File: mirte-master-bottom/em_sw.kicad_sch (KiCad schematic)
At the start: 13 parts, among them Q4 S8050 J3Y_C42441446, Q5 SiA483DJ, U11 DB125-2.54-2P-GN, U9 BZT52C18_C2932747

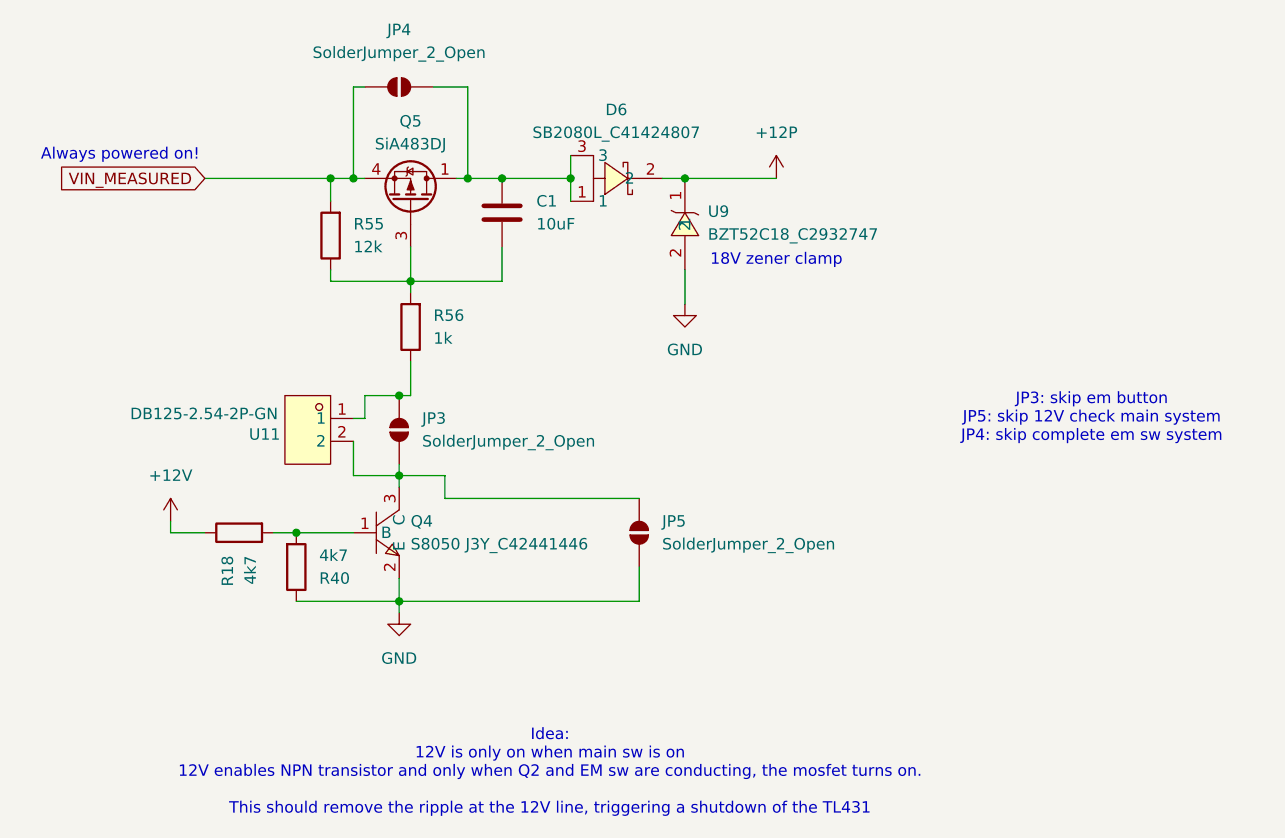
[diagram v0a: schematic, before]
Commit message: MM: ERC&DRC fixes + change hbridge cap
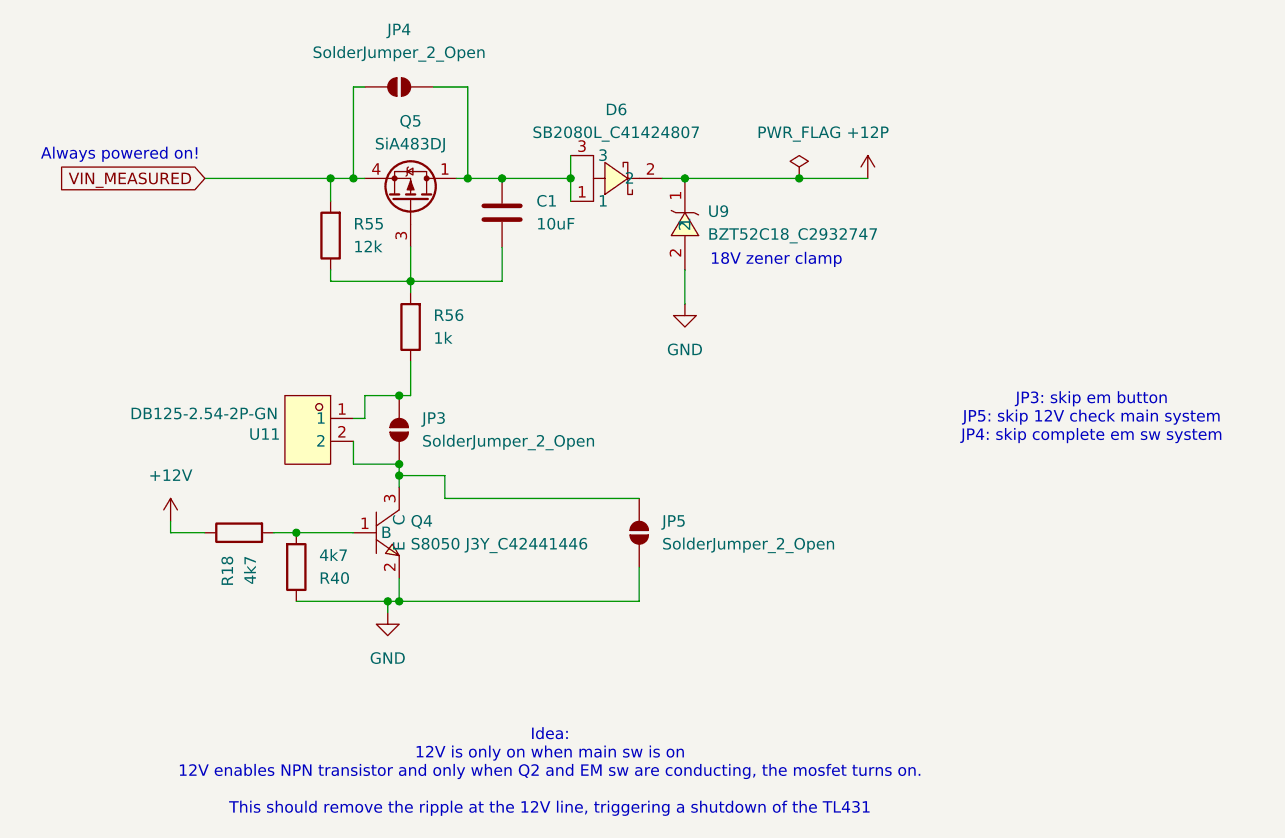
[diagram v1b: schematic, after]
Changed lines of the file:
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@@
+	)
+	(junction
+		(at 182.88 137.16)
+		(diameter 0)
+		(color 0 0 0 0)
 	)
 	(junction
@@
 	)
 	(junction
+		(at 228.6 90.17)
+		(diameter 0)
+		(color 0 0 0 0)
+	)
+	(junction
 		(at 191.77 90.17)
 		(diameter 0)
@@
 	)
 	(junction
+		(at 184.15 121.92)
+		(diameter 0)
+		(color 0 0 0 0)
+	)
+	(junction
 		(at 203.2 90.17)
 		(diameter 0)
@@
 	(wire
 		(pts
-			(xy 215.9 90.17) (xy 226.06 90.17)
+			(xy 215.9 90.17) (xy 228.6 90.17)
 		)
 		(stroke
@@
 	(wire
 		(pts
+			(xy 228.6 90.17) (xy 236.22 90.17)
+		)
+		(stroke
+			(width 0)
+			(type default)
+		)
+	)
+	(wire
+		(pts
 			(xy 170.18 129.54) (xy 172.72 129.54)
 		)
@@
 	(wire
 		(pts
-			(xy 184.15 137.16) (xy 184.15 138.43)
+			(xy 182.88 137.16) (xy 182.88 138.43)
 		)
 		(stroke
@@
 	(wire
 		(pts
-			(xy 179.07 123.19) (xy 184.15 123.19)
+			(xy 179.07 121.92) (xy 184.15 121.92)
 		)
 		(stroke
@@
 	(wire
 		(pts
+			(xy 182.88 137.16) (xy 184.15 137.16)
+		)
+		(stroke
+			(width 0)
+			(type default)
+		)
+	)
+	(wire
+		(pts
 			(xy 158.75 128.27) (xy 158.75 129.54)
 		)
@@
 	(wire
 		(pts
-			(xy 172.72 137.16) (xy 184.15 137.16)
+			(xy 172.72 137.16) (xy 182.88 137.16)
 		)
 		(stroke
@@
 	(wire
 		(pts
-			(xy 179.07 119.38) (xy 179.07 123.19)
+			(xy 179.07 119.38) (xy 179.07 121.92)
 		)
 		(stroke
@@
 	)
 	(symbol
+		(lib_id "power:PWR_FLAG")
+		(at 228.6 90.17 0)
+		(unit 1)
+		(exclude_from_sim no)
+		(in_bom yes)
+		(on_board yes)
+		(dnp no)
+		(fields_autoplaced yes)
+		(property "Reference" "#FLG01"
+			(at 228.6 88.265 0)
+			(effects
+				(font
+					(size 1.27 1.27)
+				)
+				(hide yes)
+			)
+		)
+		(property "Value" "PWR_FLAG"
+			(at 228.6 85.09 0)
+			(effects
+				(font
+					(size 1.27 1.27)
+				)
+			)
+		)
+		(property "Footprint" ""
+			(at 228.6 90.17 0)
+			(effects
+				(font
+					(size 1.27 1.27)
+				)
+				(hide yes)
+			)
+		)
+		(property "Datasheet" "~"
+			(at 228.6 90.17 0)
+			(effects
+				(font
+					(size 1.27 1.27)
+				)
+				(hide yes)
+			)
+		)
+		(property "Description" "Special symbol for telling ERC where power comes from"
+			(at 228.6 90.17 0)
+			(effects
+				(font
+					(size 1.27 1.27)
+				)
+				(hide yes)
+			)
+		)
+		(pin "1"
+		)
+		(instances
+			(project ""
+				(path "/c479422a-501d-4123-8665-56a1c70bd9ea/2572bf06-cf54-4115-a4c7-ccf0e044675d/ba374fa6-0102-4739-aefe-fc2208dddd6b"
+					(reference "#FLG01")
+					(unit 1)
+				)
+			)
+		)
+	)
+	(symbol
 		(lib_id "Device:R")
 		(at 176.53 96.52 180)
@@
 	(symbol
 		(lib_id "power:+12P")
-		(at 226.06 90.17 0)
+		(at 236.22 90.17 0)
 		(unit 1)
 		(exclude_from_sim no)
@@
 		(fields_autoplaced yes)
 		(property "Reference" "#PWR0115"
-			(at 226.06 93.98 0)
+			(at 236.22 93.98 0)
 			(effects
 				(font
@@
 		)
 		(property "Value" "+12P"
-			(at 226.06 85.09 0)
+			(at 236.22 85.09 0)
 			(effects
 				(font
@@
 		)
 		(property "Footprint" ""
-			(at 226.06 90.17 0)
+			(at 236.22 90.17 0)
 			(effects
 				(font
@@
 		)
 		(property "Datasheet" ""
-			(at 226.06 90.17 0)
+			(at 236.22 90.17 0)
 			(effects
 				(font
@@
 		)
 		(property "Description" "Power symbol creates a global label with name \"+12P\""
-			(at 226.06 90.17 0)
+			(at 236.22 90.17 0)
 			(effects
 				(font
@@
 	(symbol
 		(lib_id "power:GND")
-		(at 184.15 138.43 0)
+		(at 182.88 138.43 0)
 		(unit 1)
 		(exclude_from_sim no)
@@
 		(fields_autoplaced yes)
 		(property "Reference" "#PWR019"
-			(at 184.15 144.78 0)
+			(at 182.88 144.78 0)
 			(effects
 				(font
@@
 		)
 		(property "Value" "GND"
-			(at 184.15 143.51 0)
+			(at 182.88 143.51 0)
 			(effects
 				(font
@@
 		)
 		(property "Footprint" ""
-			(at 184.15 138.43 0)
+			(at 182.88 138.43 0)
 			(effects
 				(font
@@
 		)
 		(property "Datasheet" ""
-			(at 184.15 138.43 0)
+			(at 182.88 138.43 0)
 			(effects
 				(font
@@
 		)
 		(property "Description" "Power symbol creates a global label with name \"GND\" , ground"
-			(at 184.15 138.43 0)
-			(effects
-				(font
+			(at 182.88 138.43 0)
+			(effects
+				(font

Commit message: MM: order big
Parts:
- Q4: LCSC (none) -> C42441446
- U11: LCSC (none) -> C918120
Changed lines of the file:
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@@
+	)
+	(junction
+		(at 185.42 100.33)
+		(diameter 0)
+		(color 0 0 0 0)
 	)
 	(junction
@@
 	(wire
 		(pts
+			(xy 185.42 100.33) (xy 185.42 97.79)
+		)
+		(stroke
+			(width 0)
+			(type default)
+		)
+	)
+	(wire
+		(pts
 			(xy 191.77 80.01) (xy 187.96 80.01)
 		)
@@
 	(wire
 		(pts
-			(xy 195.58 97.79) (xy 195.58 101.6)
+			(xy 195.58 97.79) (xy 195.58 100.33)
 		)
 		(stroke
@@
 	(wire
 		(pts
-			(xy 185.42 101.6) (xy 185.42 97.79)
+			(xy 185.42 101.6) (xy 185.42 100.33)
 		)
 		(stroke
@@
 	(wire
 		(pts
-			(xy 195.58 101.6) (xy 185.42 101.6)
+			(xy 195.58 100.33) (xy 185.42 100.33)
 		)
 		(stroke
@@
 			)
 		)
+		(property "LCSC" "C42441446"
+			(at 185.42 128.2699 0)
+			(effects
+				(font
+					(size 1.27 1.27)
+				)
+				(hide yes)
+			)
+		)
 		(pin "3"
 		)
@@
 			(effects
 				(font
+					(size 1.27 1.27)
+				)
+				(hide yes)
+			)
+		)
+		(property "LCSC" "C918120"
+			(at 170.942 118.618 0)
+			(effects
+				(font
